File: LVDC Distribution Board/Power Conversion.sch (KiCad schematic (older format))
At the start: 0 parts

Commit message: Hi Frank
More schematic work. Figuring out organization mostly.
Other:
- note added: "Power Conversion"
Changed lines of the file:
@@
 $Descr A4 11693 8268
 encoding utf-8
-Sheet 1 6
+Sheet 6 6
 Title ""
 Date ""
@@
 Comment4 ""
 $EndDescr
+Text Notes 7780 7000 0    197  Italic 39
+Power Conversion
 $EndSCHEMATC

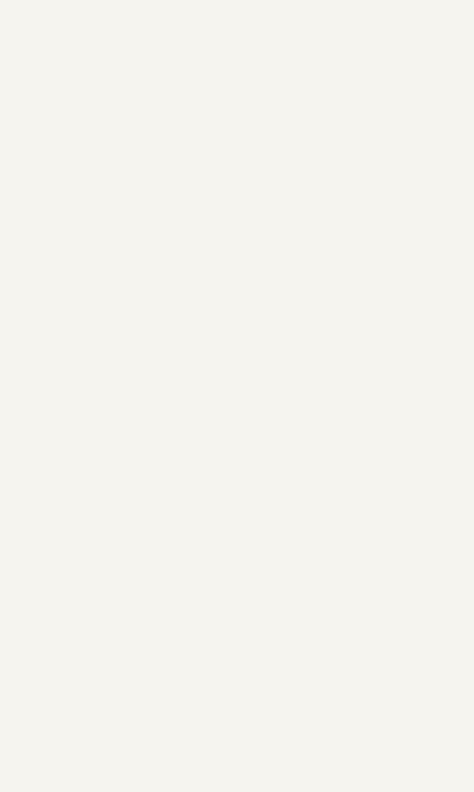
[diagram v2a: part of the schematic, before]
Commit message: Inputs / Outputs Reallyyyy Done
These two schematic sections are very finalized now. Time to do the power conversion section : - )
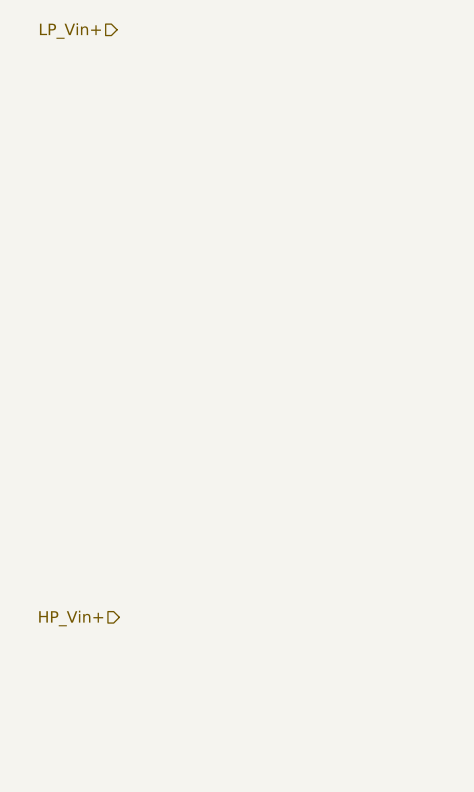
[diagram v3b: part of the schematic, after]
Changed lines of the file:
@@
 $Descr A4 11693 8268
 encoding utf-8
-Sheet 6 7
+Sheet 7 7
 Title ""
 Date ""
@@
 Text Notes 7780 7000 0    197  Italic 39
 Power Conversion
+Text HLabel 2160 1260 0    50   Input ~ 0
+LP_Vin+
+Text HLabel 2170 3830 0    50   Input ~ 0
+HP_Vin+
 $EndSCHEMATC

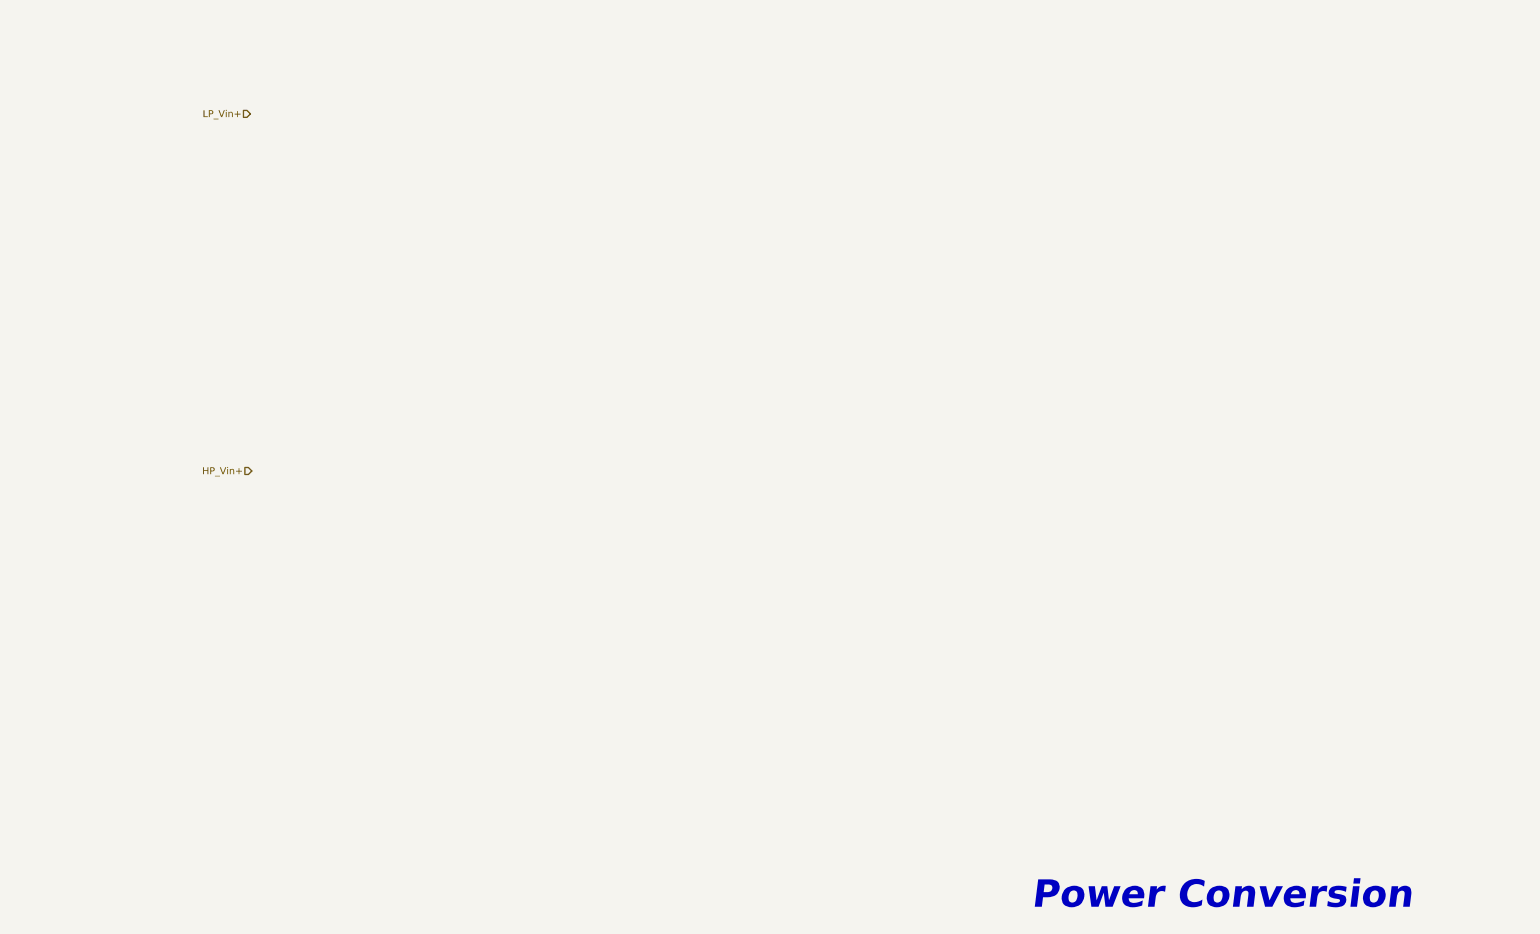
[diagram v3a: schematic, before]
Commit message: Vicor Power Converters Implemented
Big chungus vicors and associated components are spec'd and added to the schematic. Still need to add a 24V DCDC (Or LDO?) and a 3V3 LDO. Then it's on to the SAMD :+1:
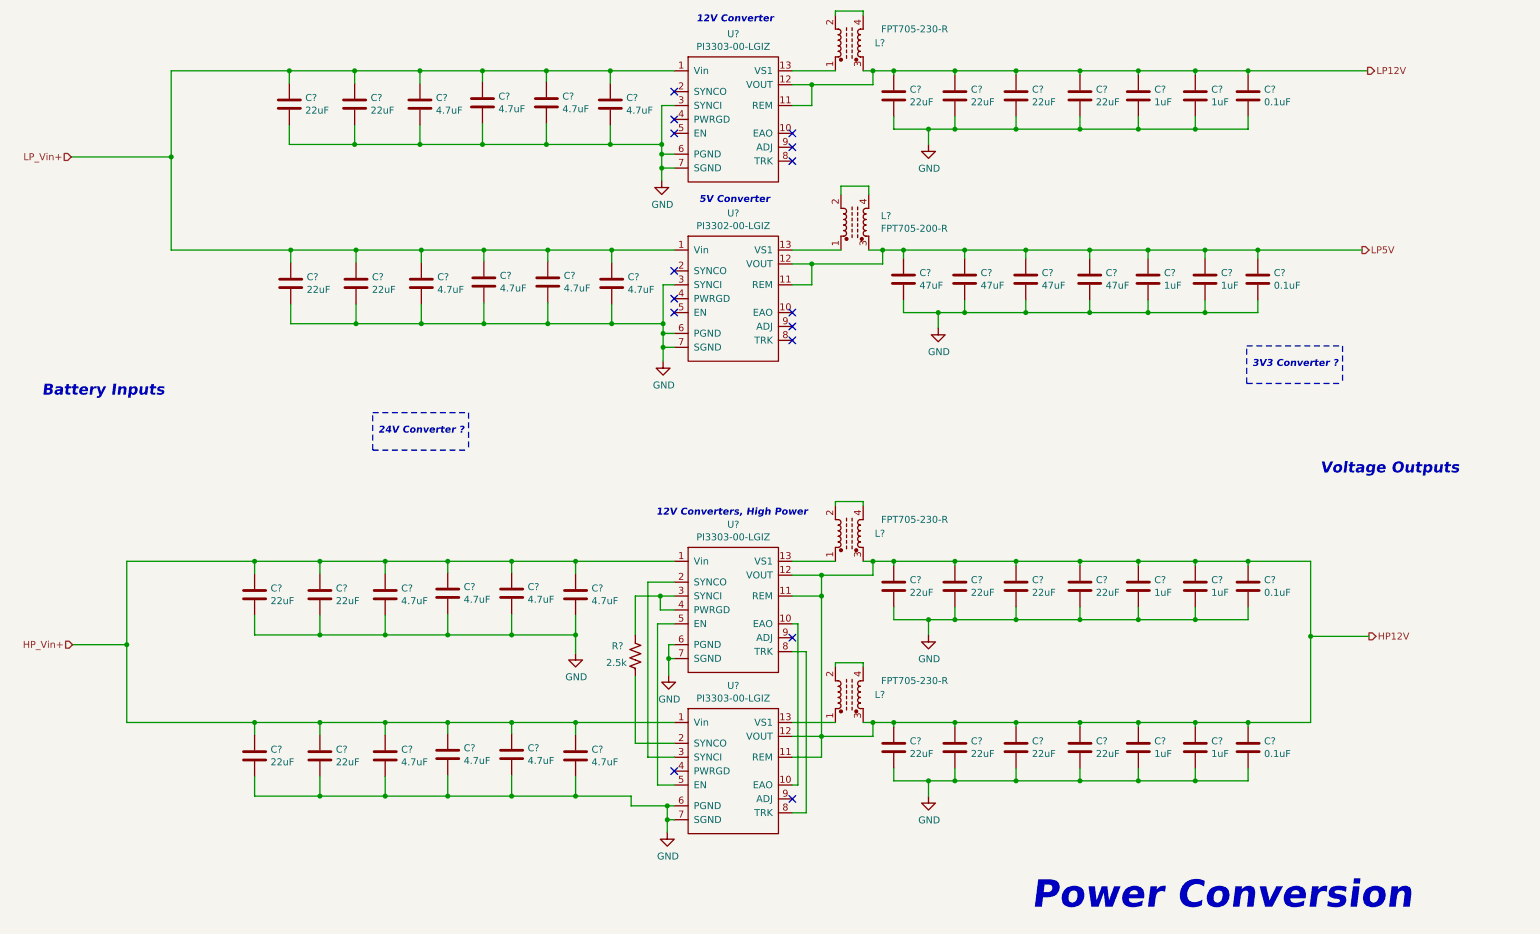
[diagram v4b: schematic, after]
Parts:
- added C? (x16): 4.7uF, symbol Device:C
- added C? (x20): 22uF, symbol Device:C
- added C? (x8): 1uF, symbol Device:C
- added C? (x4): 0.1uF, symbol Device:C
- added C? (x4): 47uF, symbol Device:C
- added L? (x3): FPT705-230-R, symbol Device:L_Core_Ferrite_Coupled
- added L?: FPT705-200-R, symbol Device:L_Core_Ferrite_Coupled
- added R?: 2.5k, symbol Device:R_US
- added U? (x3): PI3303-00-LGIZ, symbol LVDC-Library:PI33XX-00
- added U?: PI3302-00-LGIZ, symbol LVDC-Library:PI33XX-00
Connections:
- net HP_Vin+: now also C?.1, C?.1, C?.1, C?.1, C?.1, C?.1, C?.1, C?.1, C?.1, C?.1, C?.1, C?.1, U?.1 (Vin), U?.1 (Vin)
- net LP_Vin+: now also C?.1, C?.1, C?.1, C?.1, C?.1, C?.1, C?.1, C?.1, C?.1, C?.1, C?.1, C?.1, U?.1 (Vin), U?.1 (Vin)
- new net: L?.1, U?.13 (VS1) (x4)
- new net: L?.2, L?.4 (x4)
- new net: U?.10 (EAO), U?.10 (EAO)
- new net: U?.2 (SYNCO), U?.3 (SYNCI)
- new net: R?.1, U?.3 (SYNCI), U?.4 (PWRGD)
- new net: U?.5 (EN), U?.5 (EN)
- new net: U?.8 (TRK), U?.8 (TRK)
- new net: R?.2, U?.2 (SYNCO)
- new net GND: C?.2, C?.2, C?.2, C?.2, C?.2, C?.2, C?.2, C?.2, C?.2, C?.2, C?.2, C?.2, C?.2, C?.2, C?.2, C?.2, C?.2, C?.2, C?.2, C?.2, C?.2, C?.2, C?.2, C?.2, C?.2, C?.2, C?.2, C?.2, C?.2, C?.2, C?.2, C?.2, C?.2, C?.2, C?.2, C?.2, C?.2, C?.2, C?.2, C?.2, C?.2, C?.2, C?.2, C?.2, C?.2, C?.2, C?.2, C?.2, C?.2, C?.2, C?.2, C?.2, U?.3 (SYNCI), U?.3 (SYNCI), U?.6 (PGND), U?.6 (PGND), U?.6 (PGND), U?.6 (PGND), U?.7 (SGND), U?.7 (SGND), U?.7 (SGND), U?.7 (SGND)
- new net HP12V: C?.1, C?.1, C?.1, C?.1, C?.1, C?.1, C?.1, C?.1, C?.1, C?.1, C?.1, C?.1, C?.1, C?.1, L?.3, L?.3, U?.11 (REM), U?.11 (REM), U?.12 (VOUT), U?.12 (VOUT)
- new net LP12V: C?.1, C?.1, C?.1, C?.1, C?.1, C?.1, C?.1, L?.3, U?.11 (REM), U?.12 (VOUT)
- new net LP5V: C?.1, C?.1, C?.1, C?.1, C?.1, C?.1, C?.1, L?.3, U?.11 (REM), U?.12 (VOUT)
- no-connect marks 0 -> 15
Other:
- note added: "12V Converter"
- note added: "12V Converters, High Power"
- note added: "24V Converter ?"
- note added: "3V3 Converter ?"
- note added: "5V Converter"
- note added: "Battery Inputs"
- note added: "Voltage Outputs"

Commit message: Merry Chungus
Big ~Christmas~ _Chungus_ commit here boys. Rails are UP.
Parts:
- added C? (x2): 1uF, symbol Device:C
- added D? (x5): BLUE, symbol Device:LED
- added R? (x2): 4.7k, symbol Device:R_US
- added R?: 9.2k, symbol Device:R_US
- added R?: 11k, symbol Device:R_US
- added R?: 58, symbol Device:R_US
- added U?: AZ1117-3.3, symbol Regulator_Linear:AZ1117-3.3
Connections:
- net GND: now also C?.2, C?.2, D?.1 (K), D?.1 (K), D?.1 (K), D?.1 (K), D?.1 (K), U?.1 (GND)
- net HP12V: now also R?.1
- net LP12V: now also R?.1
- net LP5V: now also C?.1, R?.1, U?.3 (VI)
- new net: D?.2 (A), R?.2 (x4)
- new net: D?.2 (A), R?.1
- new net LP24V: R?.1
- new net LP3V3: C?.1, R?.2, U?.2 (VO)
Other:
- note added: "24V Converter"
- note added: "3V3 Converter"
- note removed: "24V Converter ?"
- note removed: "3V3 Converter ?"
- moved on the sheet: C?, L?, R?, U?

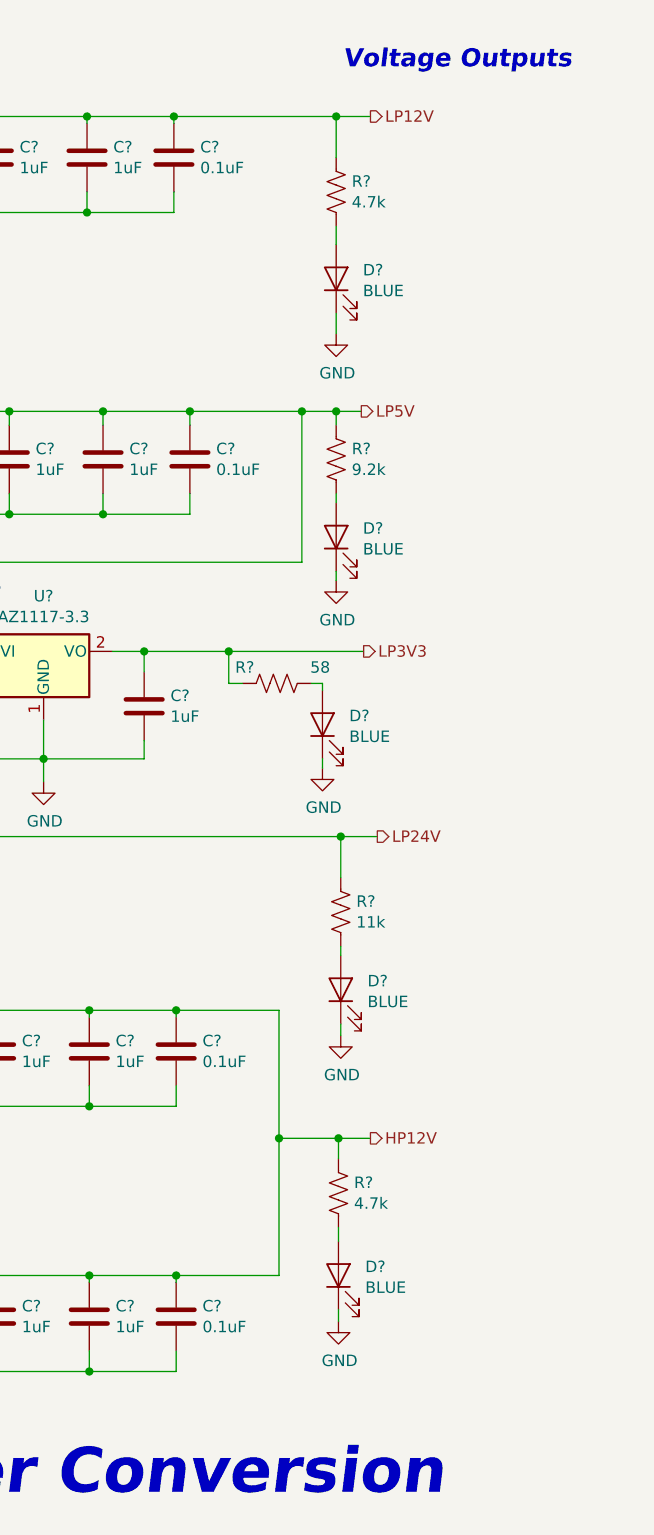
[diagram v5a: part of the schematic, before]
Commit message: SAMD21 Added
-Added VSense on rails
-Added SAMD21 and related circuits
-Mapped signals to the uC.
-Hope this is a better commit description
-Hi Frank
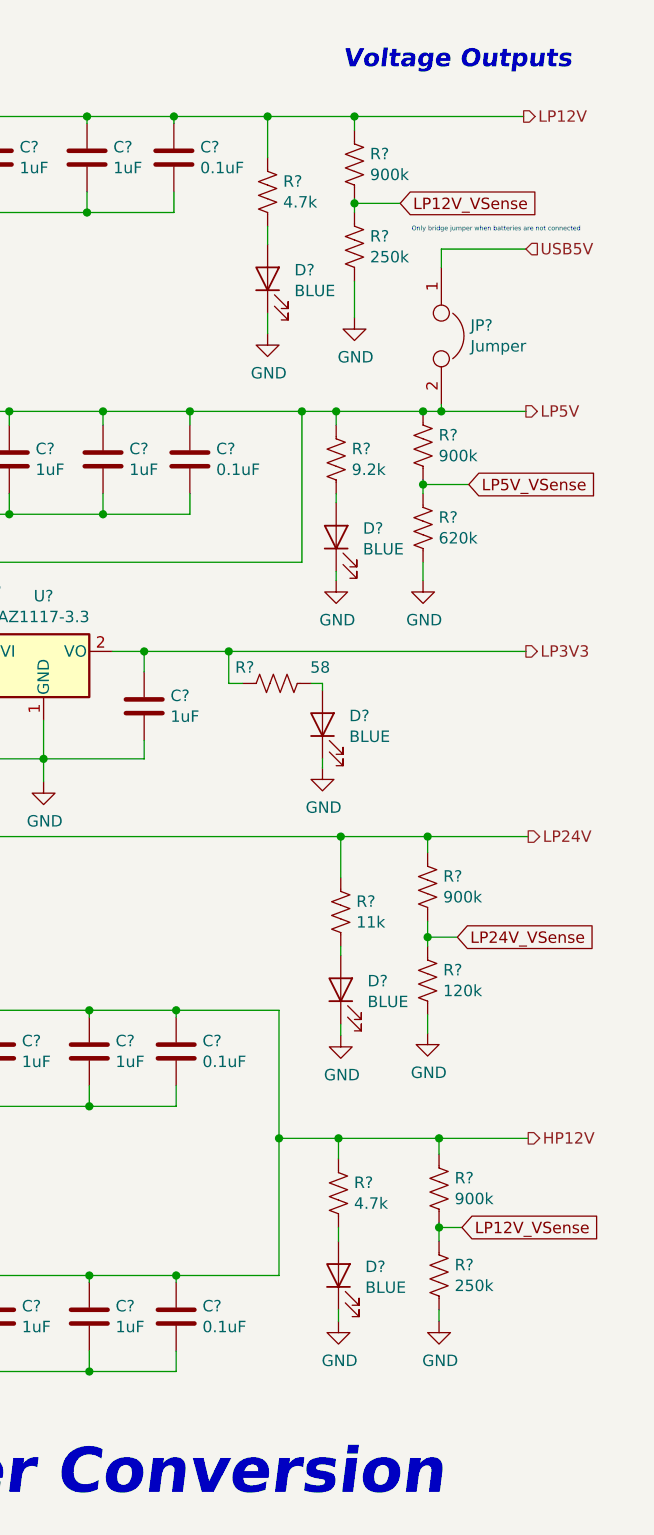
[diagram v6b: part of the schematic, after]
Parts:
- added JP?: Jumper, symbol Device:Jumper
- added R? (x4): 900k, symbol Device:R_US
- added R? (x2): 250k, symbol Device:R_US
- added R?: 620k, symbol Device:R_US
- added R?: 120k, symbol Device:R_US
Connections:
- net GND: now also R?.2, R?.2, R?.2, R?.2
- net HP12V: now also R?.1
- net LP12V: now also R?.1
- net LP24V: now also R?.1
- net LP5V: now also JP?.2, R?.1
- new net LP12V_VSense: R?.1, R?.1, R?.2, R?.2
- new net LP24V_VSense: R?.1, R?.2
- new net LP5V_VSense: R?.1, R?.2
- new net USB5V: JP?.1
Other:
- note added: "Only bridge jumper when batteries are not connected"
- moved on the sheet: D?, R?

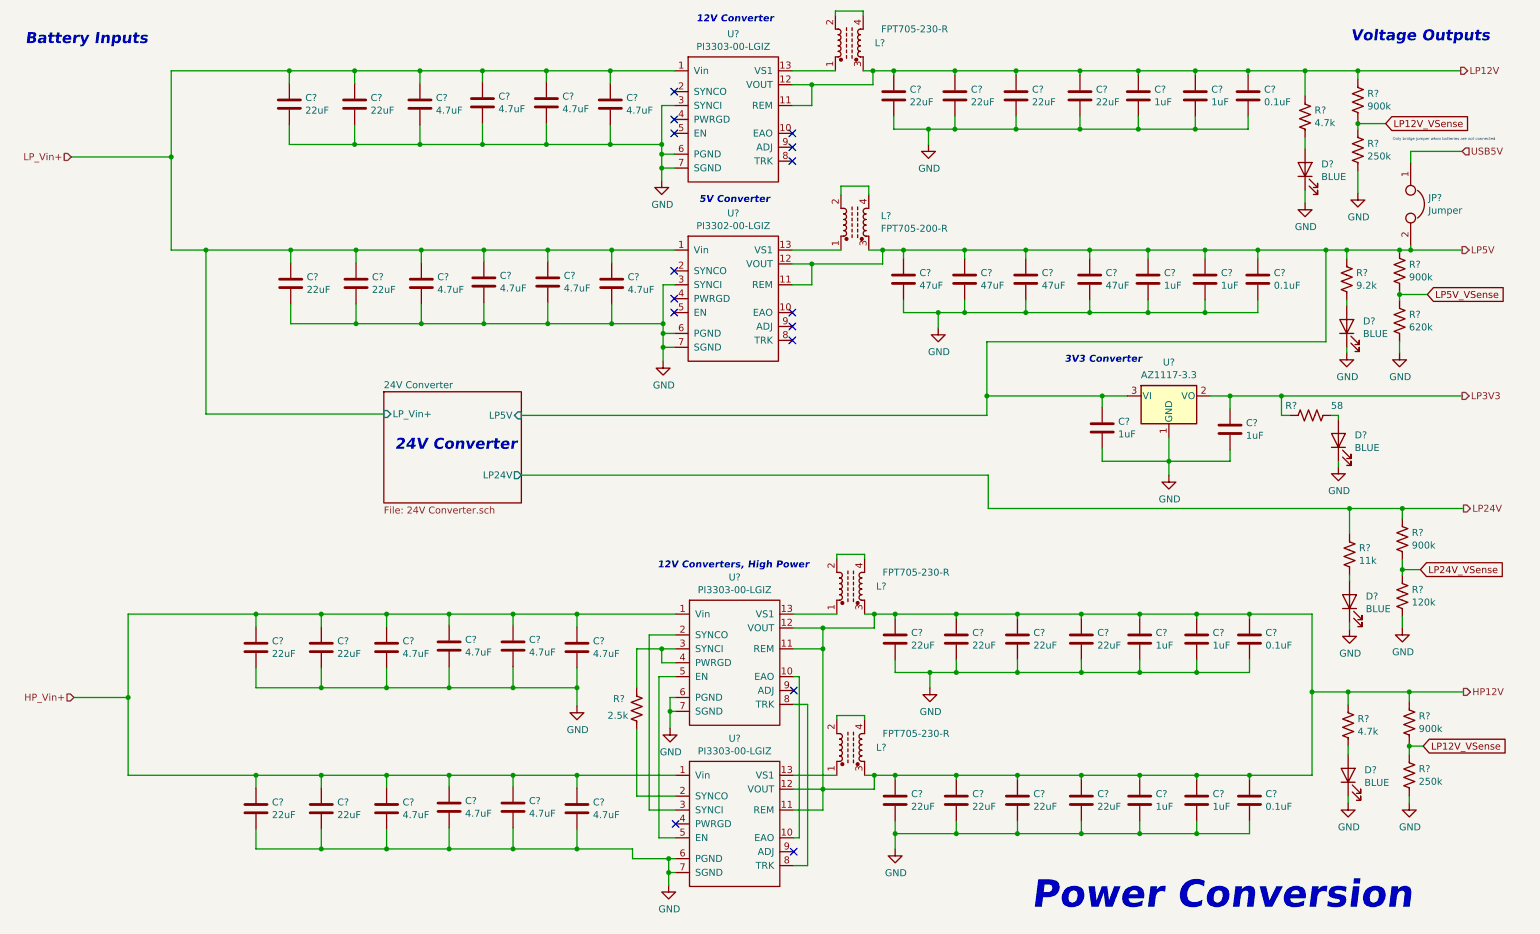
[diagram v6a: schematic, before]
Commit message: Schematic "Done"
-Added Wiznet legacy n0de schematic
-Cleaned up schematic in general
-Other than minor changes, the schematic is finalized.
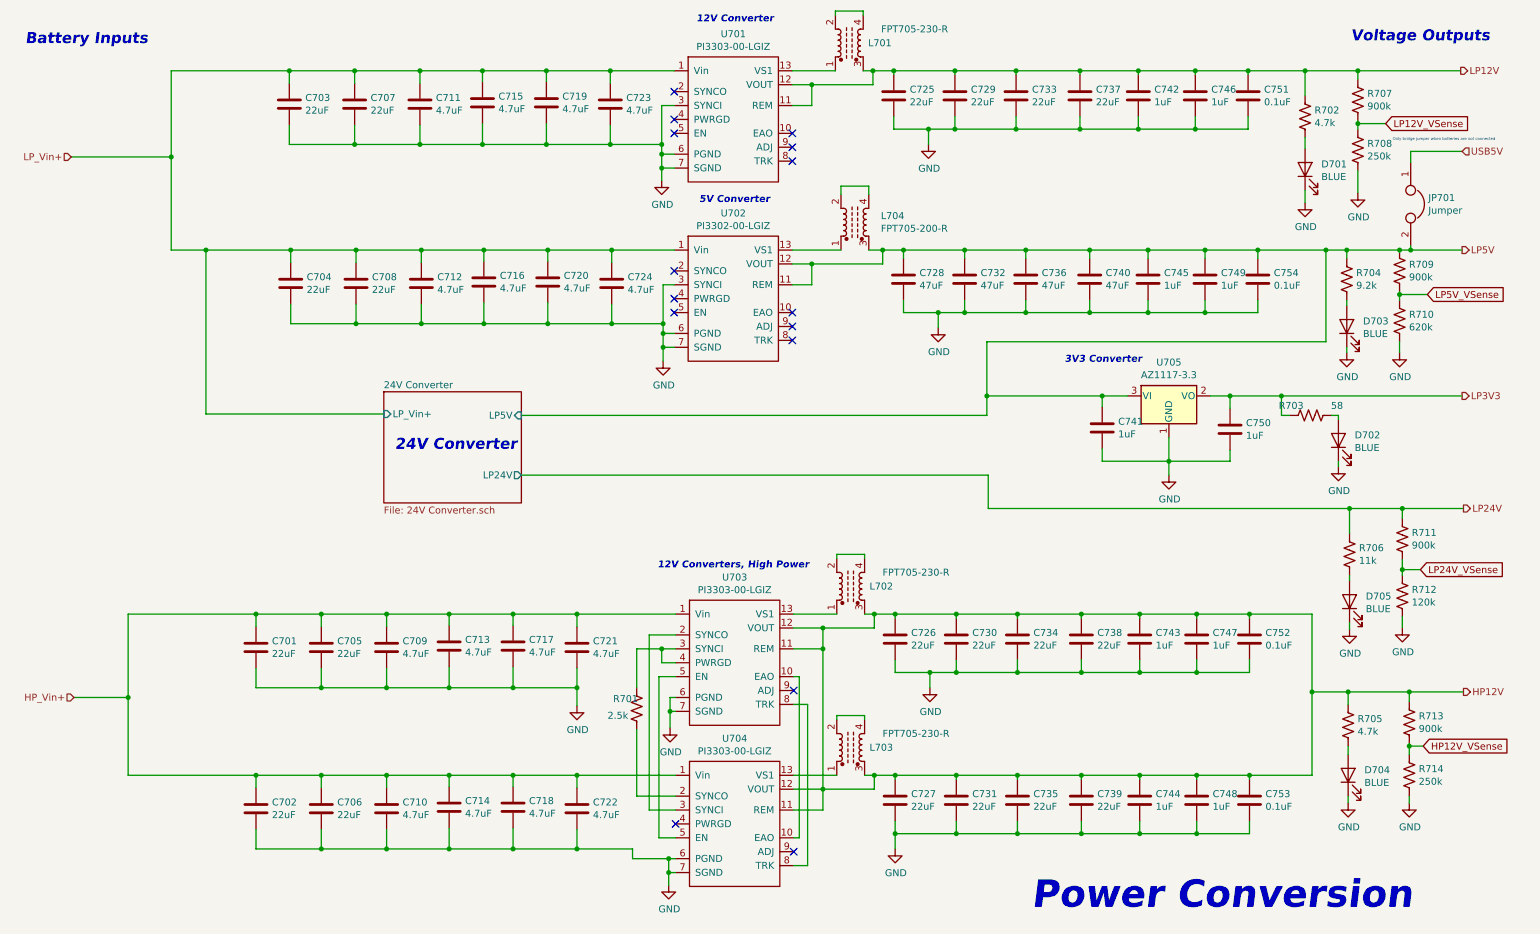
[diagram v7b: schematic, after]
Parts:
- gave numbers to parts that had none: 83
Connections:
- net LP12V_VSense: no longer R713.2, R714.1
- new net HP12V_VSense: R713.2, R714.1

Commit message: Fixed library addresses and worked on LVDC layout
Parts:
- C701, C702, C703, C704, C705, C706, C707, C708, C709, C710, C711, C712, C713, C714, C715, C716, C717, C718, C719, C720, C721, C722, C723, C724, C725, C726, C727, C728, C729, C730, C731, C732, C733, C734, C735, C736, C737, C738, C739, C740, C741, C742, C743, C744, C745, C746, C747, C748, C749, C750, C751, C752, C753, C754: footprint (none) -> Capacitor_SMD:C_0805_2012Metric_Pad1.15x1.40mm_HandSolder
- D701, D702, D703, D704, D705: footprint (none) -> LED_SMD:LED_1206_3216Metric_Pad1.42x1.75mm_HandSolder
- JP701: footprint (none) -> Resistor_SMD:R_1206_3216Metric_Pad1.42x1.75mm_HandSolder
- R701, R702, R703, R704, R705, R706, R707, R708, R709, R710, R711, R712, R713, R714: footprint (none) -> Resistor_SMD:R_0805_2012Metric_Pad1.15x1.40mm_HandSolder
- U701, U702, U703, U704: footprint (none) -> LVDC:PI330X
- U705: footprint (none) -> Package_TO_SOT_SMD:SOT-223
